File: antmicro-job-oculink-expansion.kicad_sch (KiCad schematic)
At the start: 26 parts, among them J1 OCuLink_x4_Amphenol_G14A42121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, J2 Plug_Samtec_ERM8_2x40_ERM8-04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, U1 MAX3373EEKA+

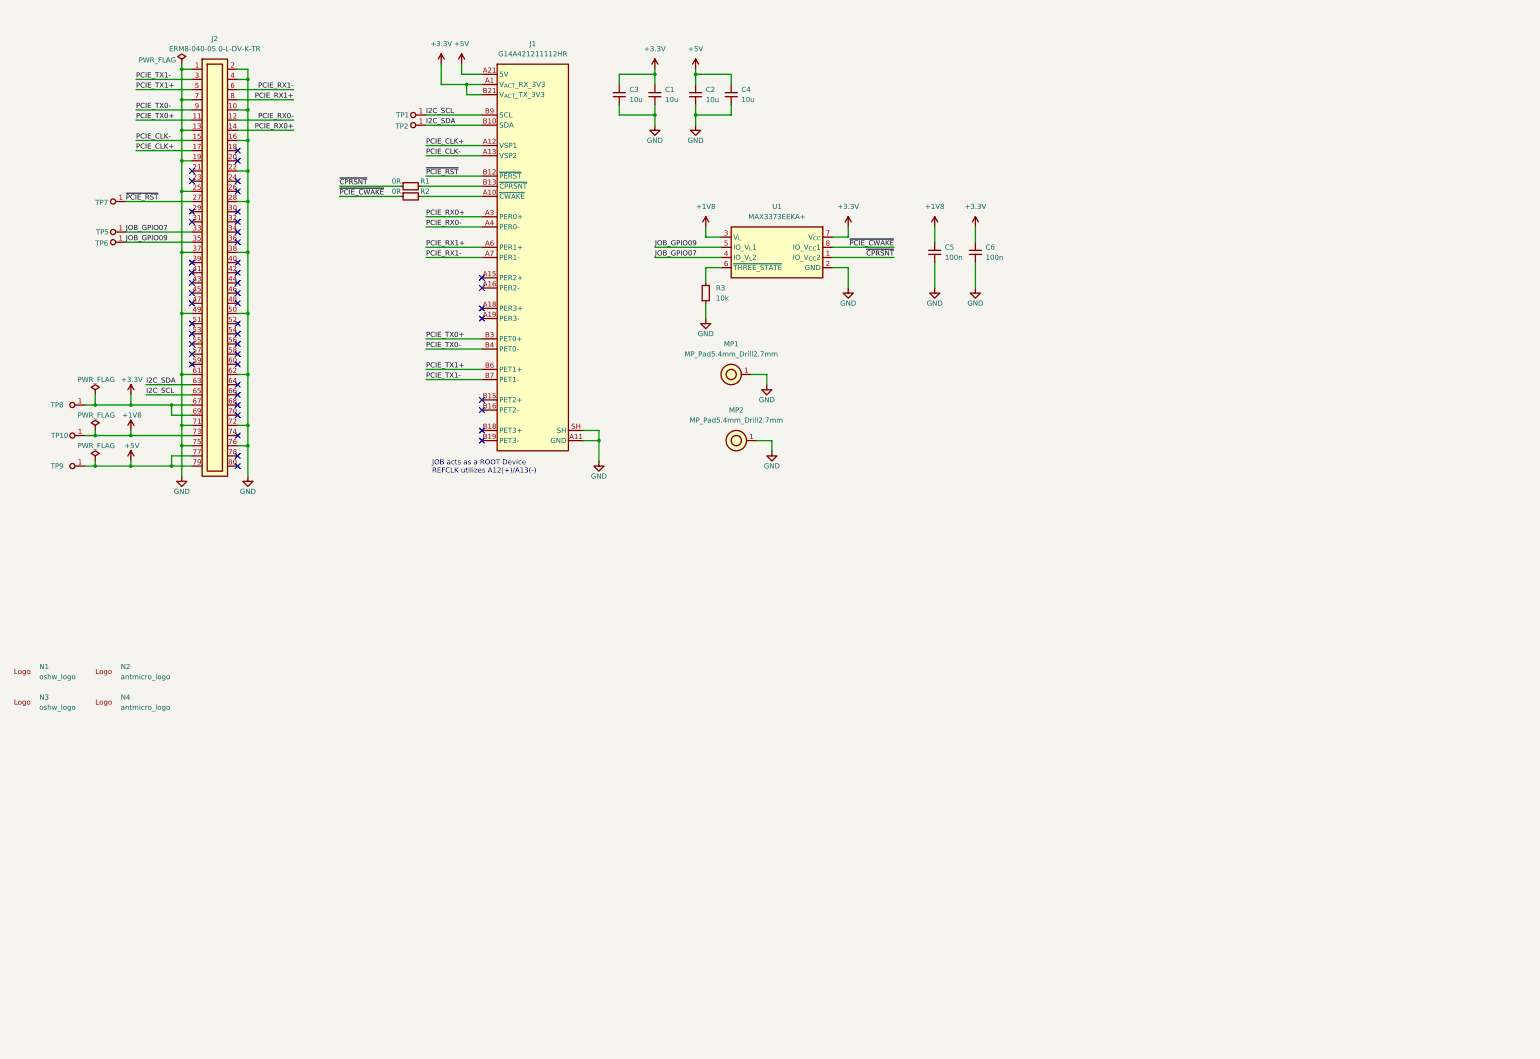
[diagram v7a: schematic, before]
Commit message: [#76297] Add PCIe redriver
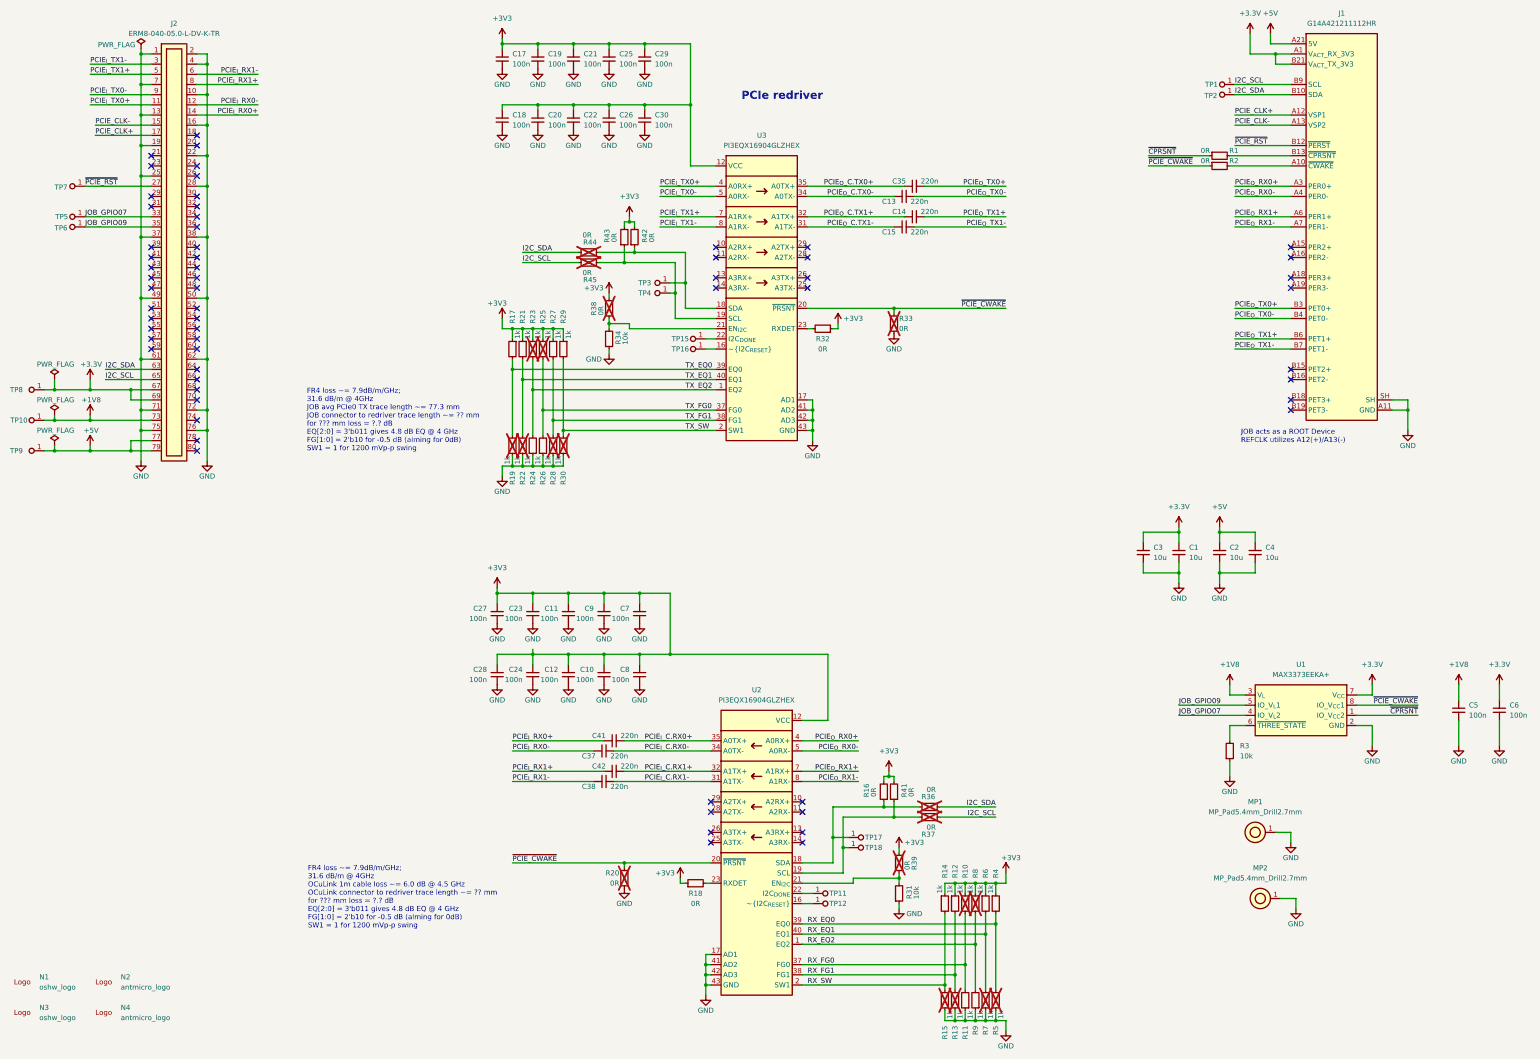
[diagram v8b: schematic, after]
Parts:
- added C10, C11, C12, C17, C18, C19, C20, C21, C22, C23, C24, C25, C26, C27, C28, C29, C30, C7, C8, C9: C_100n_0402, antmicro-footprints:C_0402_1005Metric, symbol antmicroCapacitors0402:C_100n_0402
- added C13, C14, C15, C35, C37, C38, C41, C42: C_220n_0402, antmicro-footprints:C_0402_1005Metric, symbol antmicroCapacitors0402:C_220n_0402
- added R10, R11, R12, R13, R14, R15, R17, R19, R21, R22, R23, R24, R25, R26, R27, R28, R29, R30, R4, R5, R6, R7, R8, R9: R_1k_0402, antmicro-footprints:R_0402_1005Metric, symbol antmicroResistors0402:R_1k_0402
- added R16, R18, R20, R32, R33, R36, R37, R38, R39, R41, R42, R43, R44, R45: R_0R_0402, antmicro-footprints:R_0402_1005Metric, symbol antmicroResistors0402:R_0R_0402
- added R31, R34: R_10k_0402, antmicro-footprints:R_0402_1005Metric, symbol antmicroResistors0402:R_10k_0402
- added TP11, TP12, TP15, TP16, TP17, TP18, TP3, TP4: TP_0.75mm_SMD, antmicro-footprints:TP_SMD_0.75mm, symbol antmicroTestPoints:TP_0.75mm_SMD
- added U2, U3: PI3EQX16904GL, antmicro-footprints:WQFN-42-1EP_3.5x9mm_P0.5mm, symbol antmicroInterfaceDriversReceiversTransceivers:PI3EQX16904GL
- N2, N4: footprint antmicro-footprints:antmicro-logo_scaled_15mm -> antmicro-footprints:antmicro-logo
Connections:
- net GND: now also C10.1, C11.1, C12.1, C17.1, C18.1, C19.1, C20.1, C21.1, C22.1, C23.1, C24.1, C25.1, C26.1, C27.1, C28.1, C29.1, C30.1, C7.1, C8.1, C9.1, R11.1, R13.1, R15.1, R19.1, R20.1, R22.1, R24.1, R26.1, R28.1, R30.1, R31.1, R33.1, R34.1, R5.1, R7.1, R9.1, U2.17 (AD1), U2.41 (AD2), U2.42 (AD3), U2.43 (GND), U3.17 (AD1), U3.41 (AD2), U3.42 (AD3), U3.43 (GND)
- net I2C_SCL: now also R37.1, R45.1
- net I2C_SDA: now also R36.1, R44.1
- net ~{PCIE_CWAKE}: now also R20.2, R33.2, U2.20 (~{PRSNT}), U3.20 (~{PRSNT})
- net PCIE_RX0+ renamed PCIE_{I}_RX0+
- net PCIE_{I}_RX0+: now also C41.1; no longer J1.A3 (PER0+)
- net PCIE_RX0- renamed PCIE_{I}_RX0-
- net PCIE_{I}_RX0-: now also C37.1; no longer J1.A4 (PER0-)
- net PCIE_RX1+ renamed PCIE_{I}_RX1+
- net PCIE_{I}_RX1+: now also C42.1; no longer J1.A6 (PER1+)
- net PCIE_RX1- renamed PCIE_{I}_RX1-
- net PCIE_{I}_RX1-: now also C38.1; no longer J1.A7 (PER1-)
- net PCIE_TX0+ renamed PCIE_{I}_TX0+
- net PCIE_{I}_TX0+: now also U3.4 (A0RX+); no longer J1.B3 (PET0+)
- net PCIE_TX0- renamed PCIE_{I}_TX0-
- net PCIE_{I}_TX0-: now also U3.5 (A0RX-); no longer J1.B4 (PET0-)
- net PCIE_TX1+ renamed PCIE_{I}_TX1+
- net PCIE_{I}_TX1+: now also U3.7 (A1RX+); no longer J1.B6 (PET1+)
- net PCIE_TX1- renamed PCIE_{I}_TX1-
- net PCIE_{I}_TX1-: now also U3.8 (A1RX-); no longer J1.B7 (PET1-)
- new net: R16.1, R36.2, TP17.1, U2.18 (SDA)
- new net: TP15.1, U3.22 (I2C_{DONE})
- new net: R34.2, R38.2, U3.21 (EN_{I2C})
- new net: R42.1, R44.2, TP3.1, U3.18 (SDA)
- new net: R43.1, R45.2, TP4.1, U3.19 (SCL)
- new net: R37.2, R41.1, TP18.1, U2.19 (SCL)
- new net: R31.2, R39.2, U2.21 (EN_{I2C})
- new net: R18.2, U2.23 (RXDET)
- new net: TP16.1, U3.16 (~{I2C_{RESET}})
- new net: R32.2, U3.23 (RXDET)
- new net: TP11.1, U2.22 (I2C_{DONE})
- new net: TP12.1, U2.16 (~{I2C_{RESET}})
- new net +3V3: C10.2, C11.2, C12.2, C17.2, C18.2, C19.2, C20.2, C21.2, C22.2, C23.2, C24.2, C25.2, C26.2, C27.2, C28.2, C29.2, C30.2, C7.2, C8.2, C9.2, R10.1, R12.1, R14.1, R16.2, R17.1, R18.1, R21.1, R23.1, R25.1, R27.1, R29.1, R32.1, R38.1, R39.1, R4.1, R41.2, R42.2, R43.2, R6.1, R8.1, U2.12 (VCC), U2.15 (VCC), U2.24 (VCC), U2.27 (VCC), U2.3 (VCC), U2.30 (VCC), U2.33 (VCC), U2.36 (VCC), U2.6 (VCC), U2.9 (VCC), U3.12 (VCC), U3.15 (VCC), U3.24 (VCC), U3.27 (VCC), U3.3 (VCC), U3.30 (VCC), U3.33 (VCC), U3.36 (VCC), U3.6 (VCC), U3.9 (VCC)
- new net PCIE_{I}_C.RX0+: C41.2, U2.35 (A0TX+)
- new net PCIE_{I}_C.RX0-: C37.2, U2.34 (A0TX-)
- new net PCIE_{I}_C.RX1+: C42.2, U2.32 (A1TX+)
- new net PCIE_{I}_C.RX1-: C38.2, U2.31 (A1TX-)
- new net PCIE_{O}_C.TX0+: C35.1, U3.35 (A0TX+)
- new net PCIE_{O}_C.TX0-: C13.1, U3.34 (A0TX-)
- new net PCIE_{O}_C.TX1+: C14.1, U3.32 (A1TX+)
- new net PCIE_{O}_C.TX1-: C15.1, U3.31 (A1TX-)
- new net PCIE_{O}_RX0+: J1.A3 (PER0+), U2.4 (A0RX+)
- new net PCIE_{O}_RX0-: J1.A4 (PER0-), U2.5 (A0RX-)
- new net PCIE_{O}_RX1+: J1.A6 (PER1+), U2.7 (A1RX+)
- new net PCIE_{O}_RX1-: J1.A7 (PER1-), U2.8 (A1RX-)
- new net PCIE_{O}_TX0+: C35.2, J1.B3 (PET0+)
- new net PCIE_{O}_TX0-: C13.2, J1.B4 (PET0-)
- new net PCIE_{O}_TX1+: C14.2, J1.B6 (PET1+)
- new net PCIE_{O}_TX1-: C15.2, J1.B7 (PET1-)
- new net RX_EQ0: R4.2, R5.2, U2.39 (EQ0)
- new net RX_EQ1: R6.2, R7.2, U2.40 (EQ1)
- new net RX_EQ2: R8.2, R9.2, U2.1 (EQ2)
- new net RX_FG0: R10.2, R11.2, U2.37 (FG0)
- new net RX_FG1: R12.2, R13.2, U2.38 (FG1)
- new net RX_SW: R14.2, R15.2, U2.2 (SW1)
- new net TX_EQ0: R17.2, R19.2, U3.39 (EQ0)
- new net TX_EQ1: R21.2, R22.2, U3.40 (EQ1)
- new net TX_EQ2: R23.2, R24.2, U3.1 (EQ2)
- new net TX_FG0: R25.2, R26.2, U3.37 (FG0)
- new net TX_FG1: R27.2, R28.2, U3.38 (FG1)
- new net TX_SW: R29.2, R30.2, U3.2 (SW1)
- no-connect marks 47 -> 63
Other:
- note added: "FR4 loss ~= 7.9dB/m/GHz; 31.6 dB/m @ 4GHz JOB avg PCIe0 TX trace length ~= 77.3 mm JOB connector to redriver trace length ~= ?? mm for ??? mm loss = ?.? dB EQ[2:0] = 3'b011 gives 4.8 dB EQ @ 4 GHz FG[1:0] = 2'b10 for -0.5 dB (aiming for 0dB) SW1 = 1 for 1200 mVp-p swing"
- note added: "FR4 loss ~= 7.9dB/m/GHz; 31.6 dB/m @ 4GHz OCuLink 1m cable loss ~= 6.0 dB @ 4.5 GHz OCuLink connector to redriver trace length ~= ?? mm for ??? mm loss = ?.? dB EQ[2:0] = 3'b011 gives 4.8 dB EQ @ 4 GHz FG[1:0] = 2'b10 for -0.5 dB (aiming for 0dB) SW1 = 1 for 1200 mVp-p swing"
- note added: "PCIe redriver"
- moved on the sheet: C1, C2, C3, C4, C5, C6, J1, J2, MP1, MP2, N1, N2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
